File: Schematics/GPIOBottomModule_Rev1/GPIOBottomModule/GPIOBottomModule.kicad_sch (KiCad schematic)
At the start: 11 parts, among them J1 DF40C-40DP-0.4V_51_, J2 Screw_Terminal_01x02, SW1 SW_Push, U2 BSS138

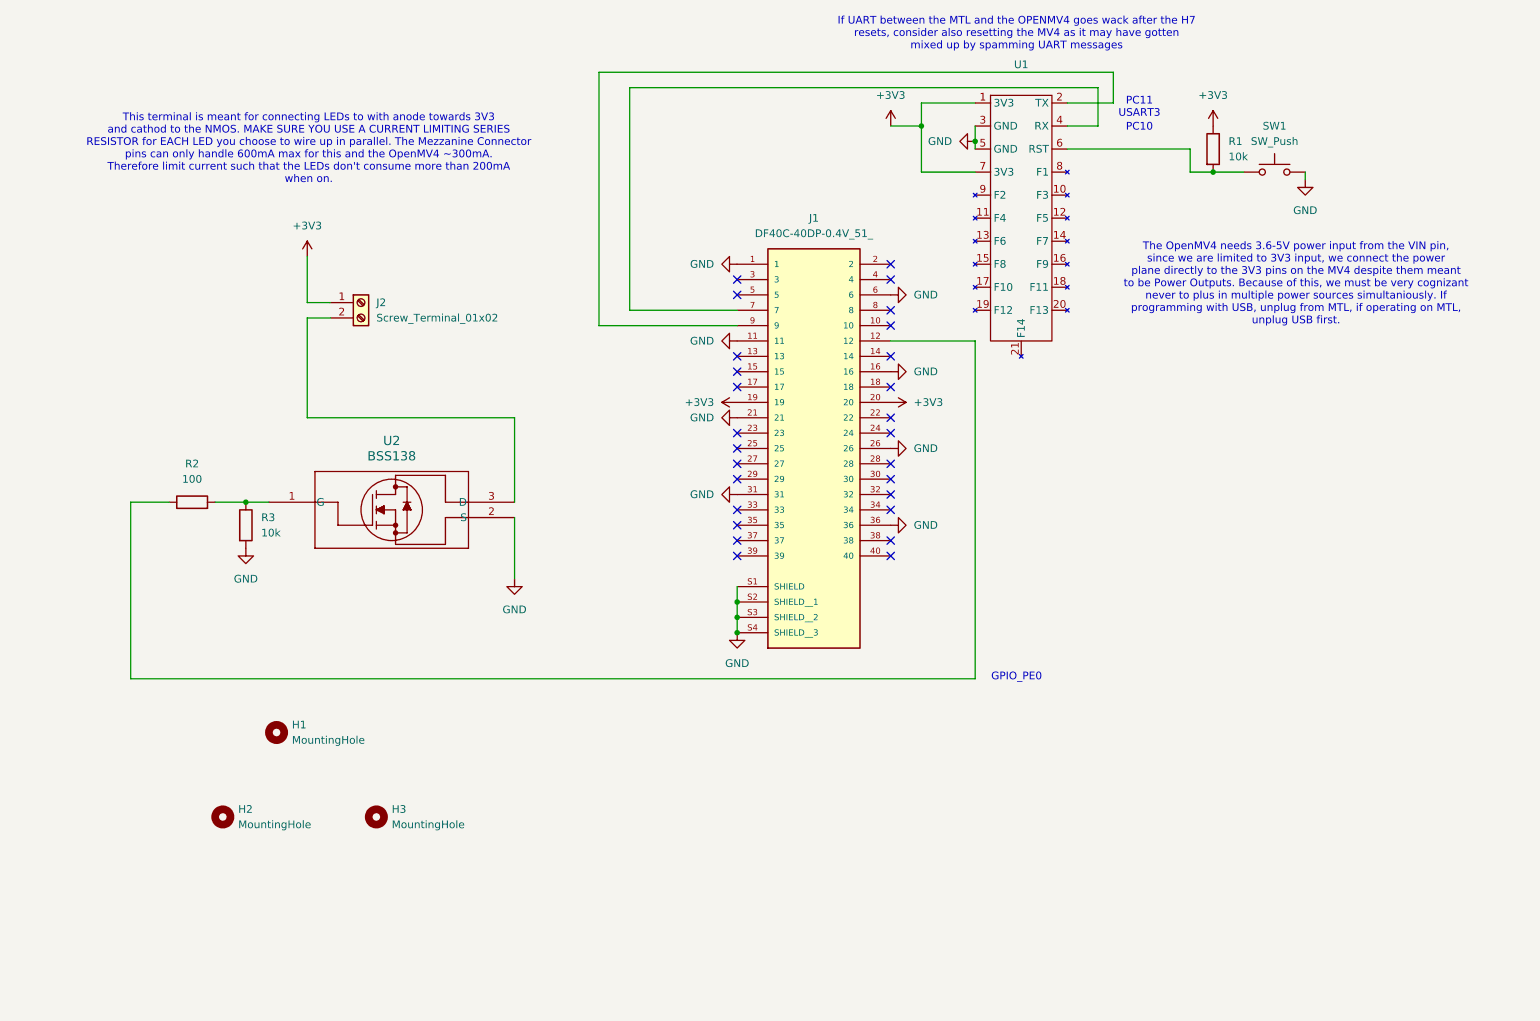
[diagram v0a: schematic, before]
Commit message: Added Bottom Module GPIO Demo board
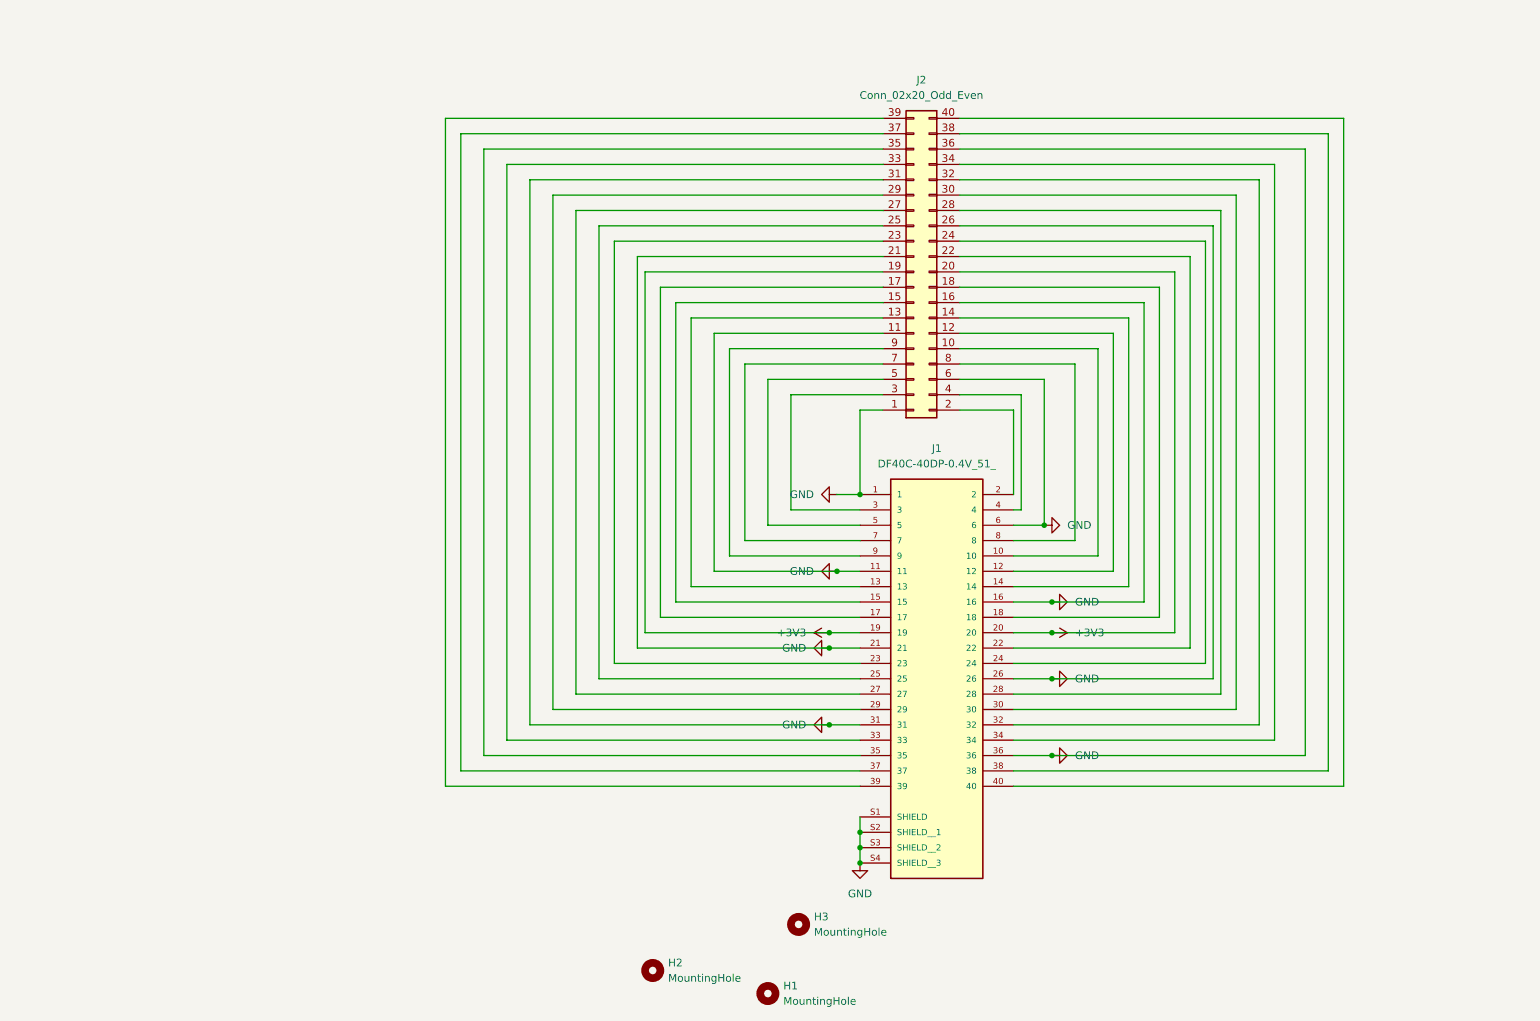
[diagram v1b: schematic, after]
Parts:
- removed J2: Screw_Terminal_01x02, TerminalBlock_Phoenix:TerminalBlock_Phoenix_MKDS-1,5-2-5.08_1x02_P5.08mm_Horizontal, symbol Connector:Screw_Terminal_01x02
- removed R1, R3: 10k, Resistor_SMD:R_0805_2012Metric_Pad1.20x1.40mm_HandSolder, symbol Device:R
- removed R2: 100, Resistor_SMD:R_0805_2012Metric_Pad1.20x1.40mm_HandSolder, symbol Device:R
- removed SW1: SW_Push, Button_Switch_SMD:SW_SPST_PTS645Sx43SMTR92, symbol Switch:SW_Push
- removed U1: ~, CustomFootprints:OPENMV4_H7, symbol Custom_Symbols:OPENMV4_CAM_H7
- removed U2: BSS138, BSS138:SOT-23_3L_ONS-M, symbol BSS138:BSS138
- added J2: Conn_02x20_Odd_Even, Connector_PinHeader_2.54mm:PinHeader_2x20_P2.54mm_Vertical, symbol Connector_Generic:Conn_02x20_Odd_Even
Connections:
- net +3V3: now also J2.19 (Pin_19), J2.20 (Pin_20)
- net GND: now also J2.1 (Pin_1), J2.11 (Pin_11), J2.16 (Pin_16), J2.21 (Pin_21), J2.26 (Pin_26), J2.31 (Pin_31), J2.36 (Pin_36), J2.6 (Pin_6)
- net at J1.10: now also J2.10 (Pin_10)
- net at J1.12: now also J2.12 (Pin_12)
- net at J1.13: now also J2.13 (Pin_13)
- net at J1.14: now also J2.14 (Pin_14)
- net at J1.15: now also J2.15 (Pin_15)
- net at J1.17: now also J2.17 (Pin_17)
- net at J1.18: now also J2.18 (Pin_18)
- net at J1.2: now also J2.2 (Pin_2)
- net at J1.22: now also J2.22 (Pin_22)
- net at J1.23: now also J2.23 (Pin_23)
- net at J1.24: now also J2.24 (Pin_24)
- net at J1.25: now also J2.25 (Pin_25)
- net at J1.27: now also J2.27 (Pin_27)
- net at J1.28: now also J2.28 (Pin_28)
- net at J1.29: now also J2.29 (Pin_29)
- net at J1.3: now also J2.3 (Pin_3)
- net at J1.30: now also J2.30 (Pin_30)
- net at J1.32: now also J2.32 (Pin_32)
- net at J1.33: now also J2.33 (Pin_33)
- net at J1.34: now also J2.34 (Pin_34)
- net at J1.35: now also J2.35 (Pin_35)
- net at J1.37: now also J2.37 (Pin_37)
- net at J1.38: now also J2.38 (Pin_38)
- net at J1.39: now also J2.39 (Pin_39)
- net at J1.4: now also J2.4 (Pin_4)
- net at J1.40: now also J2.40 (Pin_40)
- net at J1.5: now also J2.5 (Pin_5)
- net at J1.7: now also J2.7 (Pin_7)
- net at J1.8: now also J2.8 (Pin_8)
- net at J1.9: now also J2.9 (Pin_9)
- no-connect marks 27 -> 0
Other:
- note removed: "GPIO_PE0"
- note removed: "If UART between the MTL and the OPENMV4 goes wack after the H7 resets, consider also resetting the MV4 as it may have gotten mixed up by spamming UART messages"
- note removed: "PC10"
- note removed: "PC11"
- note removed: "The OpenMV4 needs 3.6-5V power input from the VIN pin, since we are limited to 3V3 input, we connect the power plane directly to the 3V3 pins on the MV4 despite them meant to be Power Outputs. Because of this, we must be very cognizant never to plus in multiple power sources simultaniously. If programming with USB, unplug from MTL, if operating on MTL, unplug USB first."
- note removed: "This terminal is meant for connecting LEDs to with anode towards 3V3 and cathod to the NMOS. MAKE SURE YOU USE A CURRENT LIMITING SERIES RESISTOR for EACH LED you choose to wire up in parallel. The Mezzanine Connector pins can only handle 600mA max for this and the OpenMV4 ~300mA. Therefore limit current such that the LEDs don't consume more than 200mA when on."
- note removed: "USART3"
- moved on the sheet: H1, H2, H3, J1
